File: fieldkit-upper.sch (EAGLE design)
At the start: 52 parts, among them J1 TAG-CONNECT, U1 TC58CVG1S3HRAIG, U2 TC58CVG1S3HRAIG, U3 TC58CVG1S3HRAIG, U4 TC58CVG1S3HRAIG

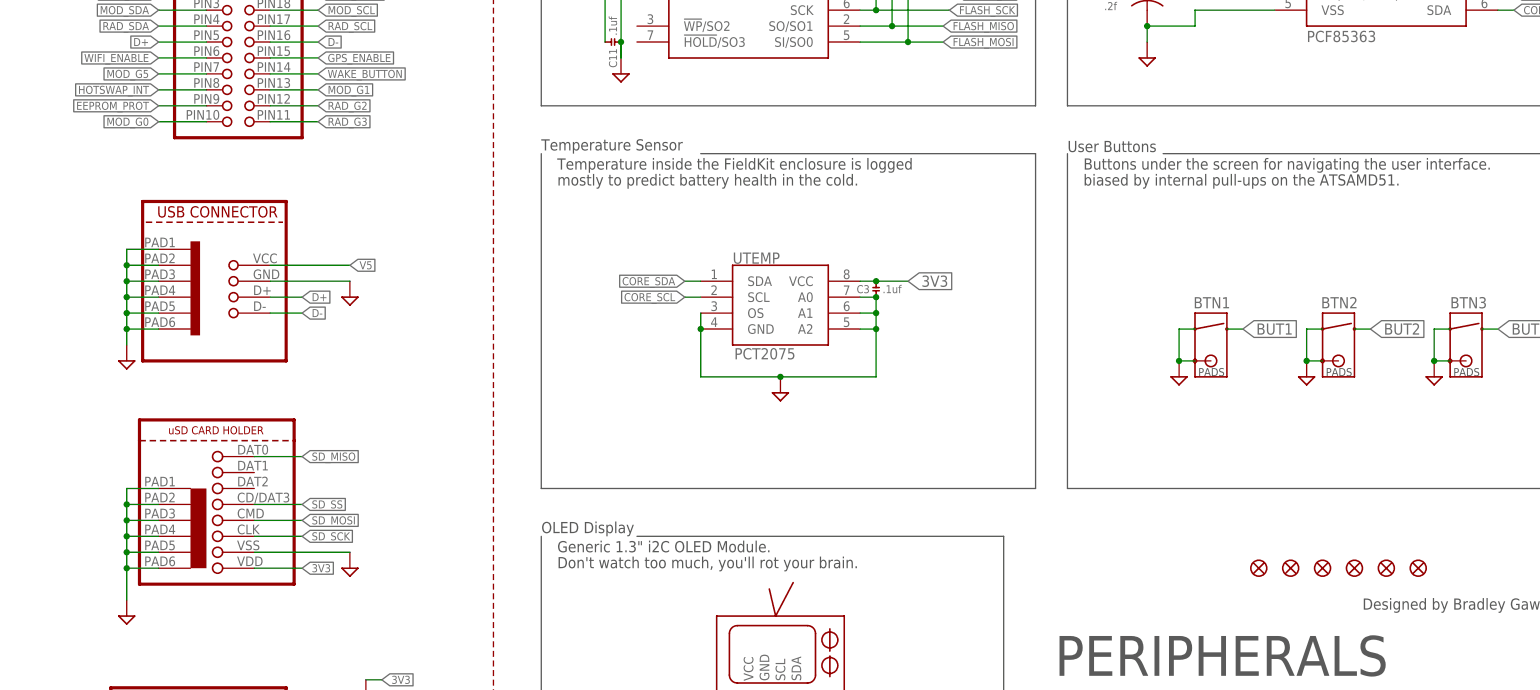
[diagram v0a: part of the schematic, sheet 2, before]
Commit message: Routing cleanup, pin nomenclature fixes.
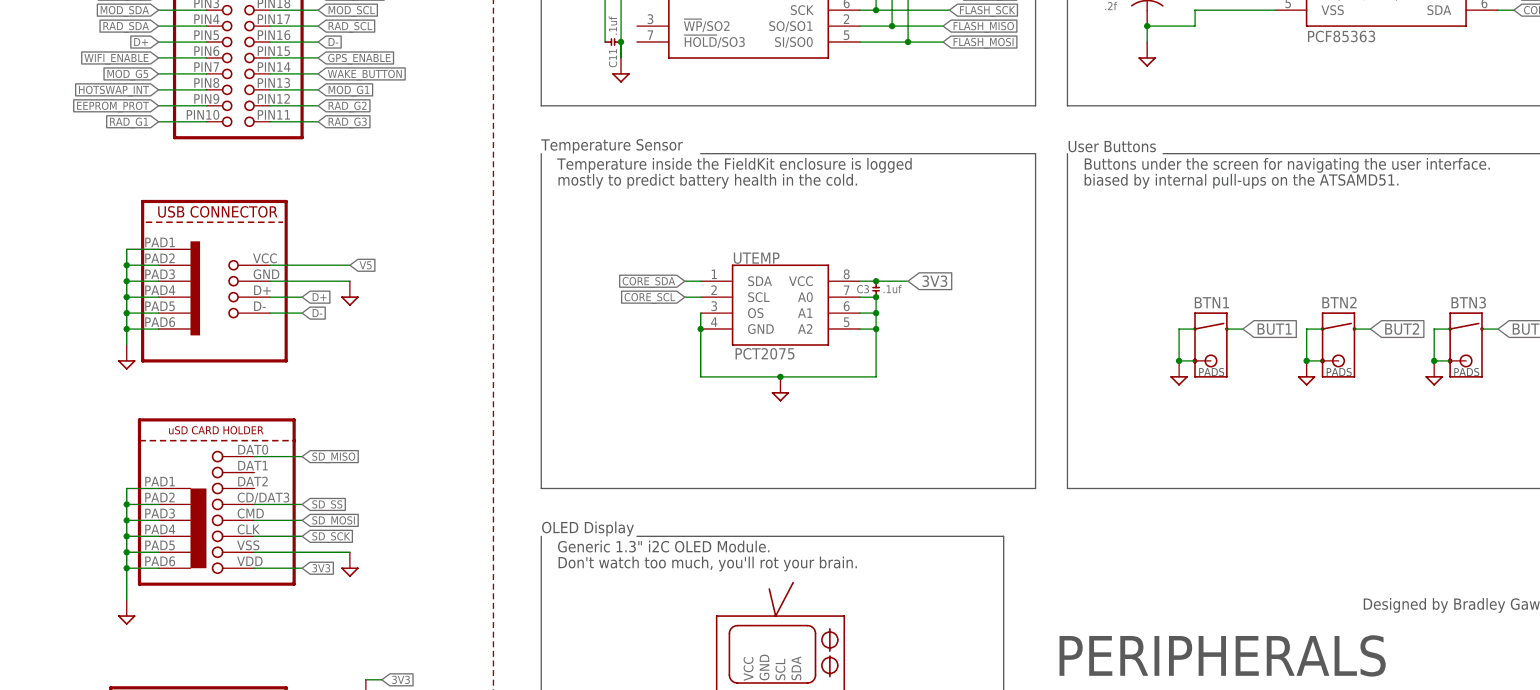
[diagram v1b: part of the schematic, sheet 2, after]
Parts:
- removed FID1, FID2, FID3, FID4, FID5, FID6: FIDUCIAL_1MM, microbuilder:FIDUCIAL_1MM
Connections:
- removed net MOD_G0: LOWER.PIN10
- net RAD_G1: now also LOWER.PIN10
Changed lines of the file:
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@@
 <setting verticaltext="up"/>
 </settings>
-<grid distance="0.1" unitdist="inch" unit="inch" style="lines" multiple="1" display="no" altdistance="0.01" altunitdist="inch" altunit="inch"/>
+<grid distance="1" unitdist="inch" unit="mm" style="lines" multiple="1" display="no" altdistance="0.01" altunitdist="inch" altunit="inch"/>
 <layers>
 <layer number="1" name="Top" color="4" fill="1" visible="no" active="no"/>
@@
 <layer number="255" name="routoute" color="7" fill="1" visible="yes" active="yes"/>
 </layers>
-<schematic xreflabel="%F%N" xrefpart="/%S.%C%R">
+<schematic xreflabel="%F%N/%S.%C%R" xrefpart="/%S.%C%R">
 <attributes>
 </attributes>
@@
 <part name="C7" library="rcl" library_urn="urn:adsk.eagle:library:334" deviceset="C-US" device="C0603K" package3d_urn="urn:adsk.eagle:package:23680/2" value="4.7uf"/>
 <part name="R5" library="rcl" library_urn="urn:adsk.eagle:library:334" deviceset="R-US_" device="R0603" package3d_urn="urn:adsk.eagle:package:23555/3" value="10K"/>
-<part name="FID1" library="microbuilder" deviceset="FIDUCIAL" device="_1MM"/>
-<part name="FID2" library="microbuilder" deviceset="FIDUCIAL" device="_1MM"/>
-<part name="FID3" library="microbuilder" deviceset="FIDUCIAL" device="_1MM"/>
-<part name="FID4" library="microbuilder" deviceset="FIDUCIAL" device="_1MM"/>
-<part name="FID5" library="microbuilder" deviceset="FIDUCIAL" device="_1MM"/>
-<part name="FID6" library="microbuilder" deviceset="FIDUCIAL" device="_1MM"/>
 <part name="J1" library="Conservify" library_urn="urn:adsk.eagle:library:11839183" deviceset="TAG-CONNECT" device="" package3d_urn="urn:adsk.eagle:package:16969550/1"/>
 <part name="R6" library="rcl" library_urn="urn:adsk.eagle:library:334" deviceset="R-US_" device="R0603" package3d_urn="urn:adsk.eagle:package:23555/3" value="10k"/>
@@
 <instance part="SUPPLY13" gate="GND" x="22.86" y="12.7" smashed="yes"/>
 <instance part="SUPPLY14" gate="GND" x="129.54" y="10.16" smashed="yes"/>
-<instance part="FID1" gate="G$1" x="208.28" y="43.18" smashed="yes" rot="R90"/>
-<instance part="FID2" gate="G$1" x="213.36" y="43.18" smashed="yes" rot="R90"/>
-<instance part="FID3" gate="G$1" x="218.44" y="43.18" smashed="yes" rot="R90"/>
-<instance part="FID4" gate="G$1" x="223.52" y="43.18" smashed="yes" rot="R90"/>
-<instance part="FID5" gate="G$1" x="228.6" y="43.18" smashed="yes" rot="R90"/>
-<instance part="FID6" gate="G$1" x="233.68" y="43.18" smashed="yes" rot="R90"/>
 </instances>
 <busses>
@@
 </segment>
 </net>
-<net name="MOD_G0" class="0">
+<net name="RAD_G1" class="0">
 <segment>
 <pinref part="LOWER" gate="G$1" pin="PIN10"/>
